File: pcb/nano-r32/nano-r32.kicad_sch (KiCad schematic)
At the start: 15 parts, among them J1 USB_A, J2 Conn_01x14_Pin, J3 Conn_01x14_Pin, U1 CH32X035G8R6

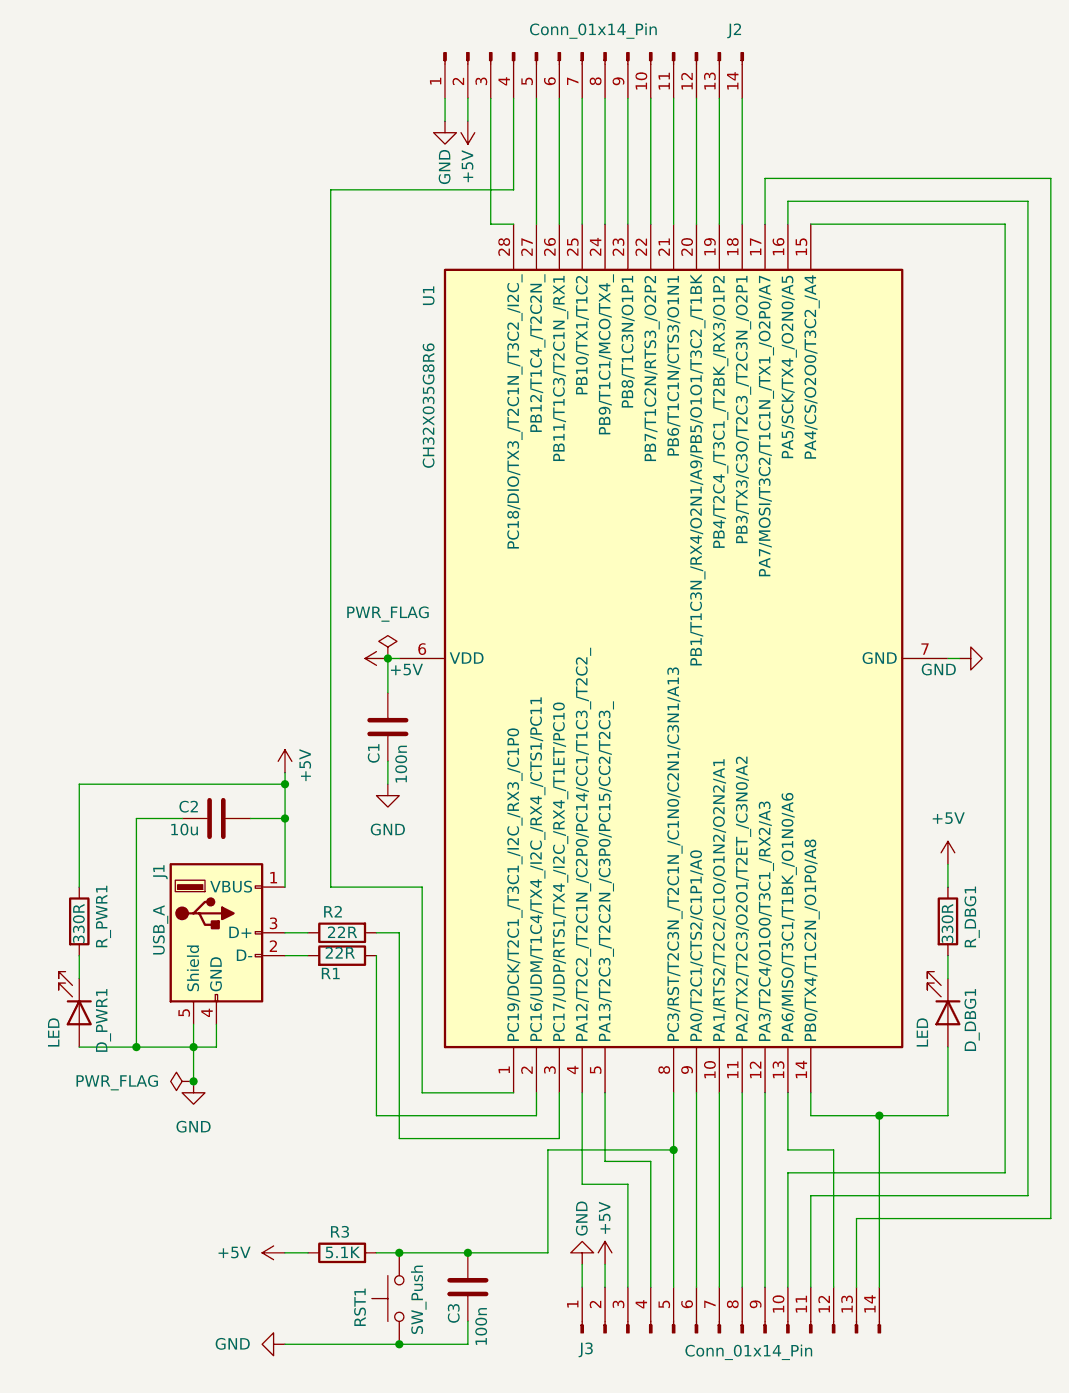
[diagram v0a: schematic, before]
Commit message: update debug board schematic and layout: add boot button, fix led polarity
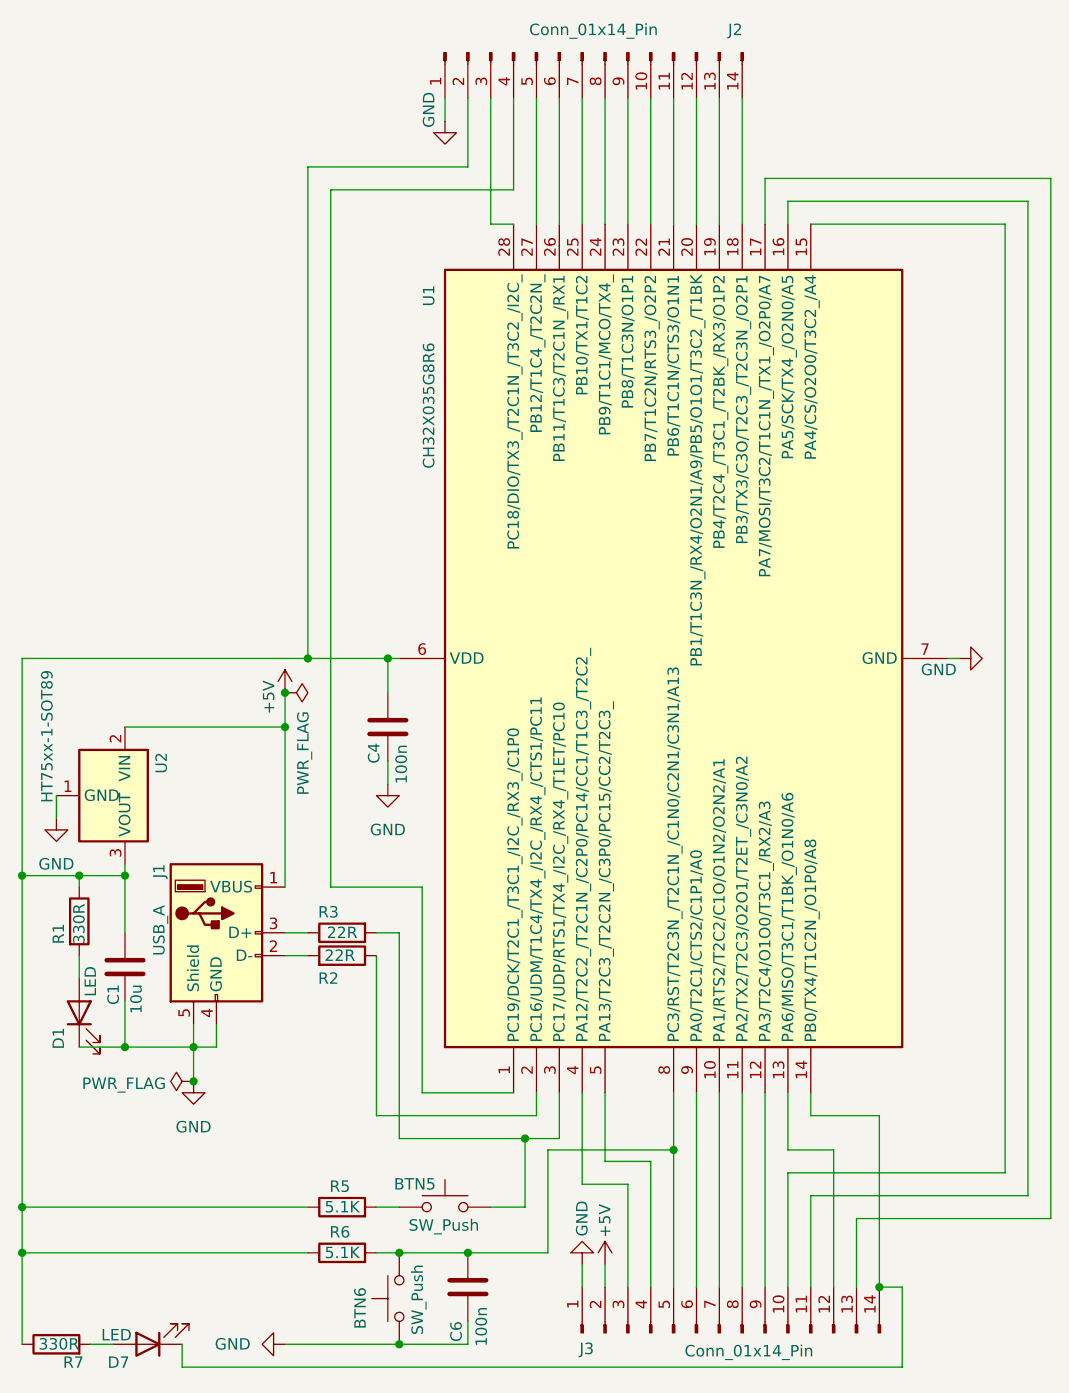
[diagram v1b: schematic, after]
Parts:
- removed D_DBG1: LED, Diode_SMD:D_1206_3216Metric, symbol Device:LED
- removed R_DBG1: 330R, Resistor_SMD:R_0805_2012Metric, symbol Device:R
- added BTN5: SW_Push, Button_Switch_SMD:SW_SPST_5x5x1.5, symbol Switch:SW_Push
- added D7: LED, Diode_SMD:D_1206_3216Metric, symbol Device:LED
- added R5: 5.1K, Resistor_SMD:R_0805_2012Metric, symbol Device:R
- added R7: 330R, Resistor_SMD:R_0805_2012Metric, symbol Device:R
- added U2: HT75xx-1-SOT89, Package_TO_SOT_SMD:SOT-89-3, symbol Regulator_Linear:HT75xx-1-SOT89
- renumbered RST1 to BTN6, C2 to C1, C1 to C4, C3 to C6, D_PWR1 to D1, R_PWR1 to R1, R1 to R2, R2 to R3, R3 to R6
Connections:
- net +5V: now also U2.2 (VIN); no longer C1.2, C4.1, J2.2 (Pin_2), R1.1, R6.1, U1.6 (VDD)
- net GND: now also D1.1 (K), U2.1 (GND); no longer D1.2 (A)
- net at J3.14 (Pin_14), U1.14 (PB0/TX4/T1C2N_/O1P0/A8): now also D7.1 (K)
- net at R3.2, U1.3 (PC17/UDP/RTS1/TX4_/I2C_/RX4_/T1ET/PC10): now also BTN5.2
- net at R1.2: now also D1.2 (A); no longer D1.1 (K)
- new net: C1.2, C4.1, J2.2 (Pin_2), R1.1, R5.1, R6.1, R7.1, U1.6 (VDD), U2.3 (VOUT)
- new net: BTN5.1, R5.2
- new net: D7.2 (A), R7.2
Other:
- moved on the sheet: C1, D1
